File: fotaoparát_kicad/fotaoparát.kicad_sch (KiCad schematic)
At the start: 13 parts, among them IC1 W25Q256JVEIQ, J1 Conn_01x15_Pin, J2 Micro_SD_Card_Det1, Q1 AO3400A

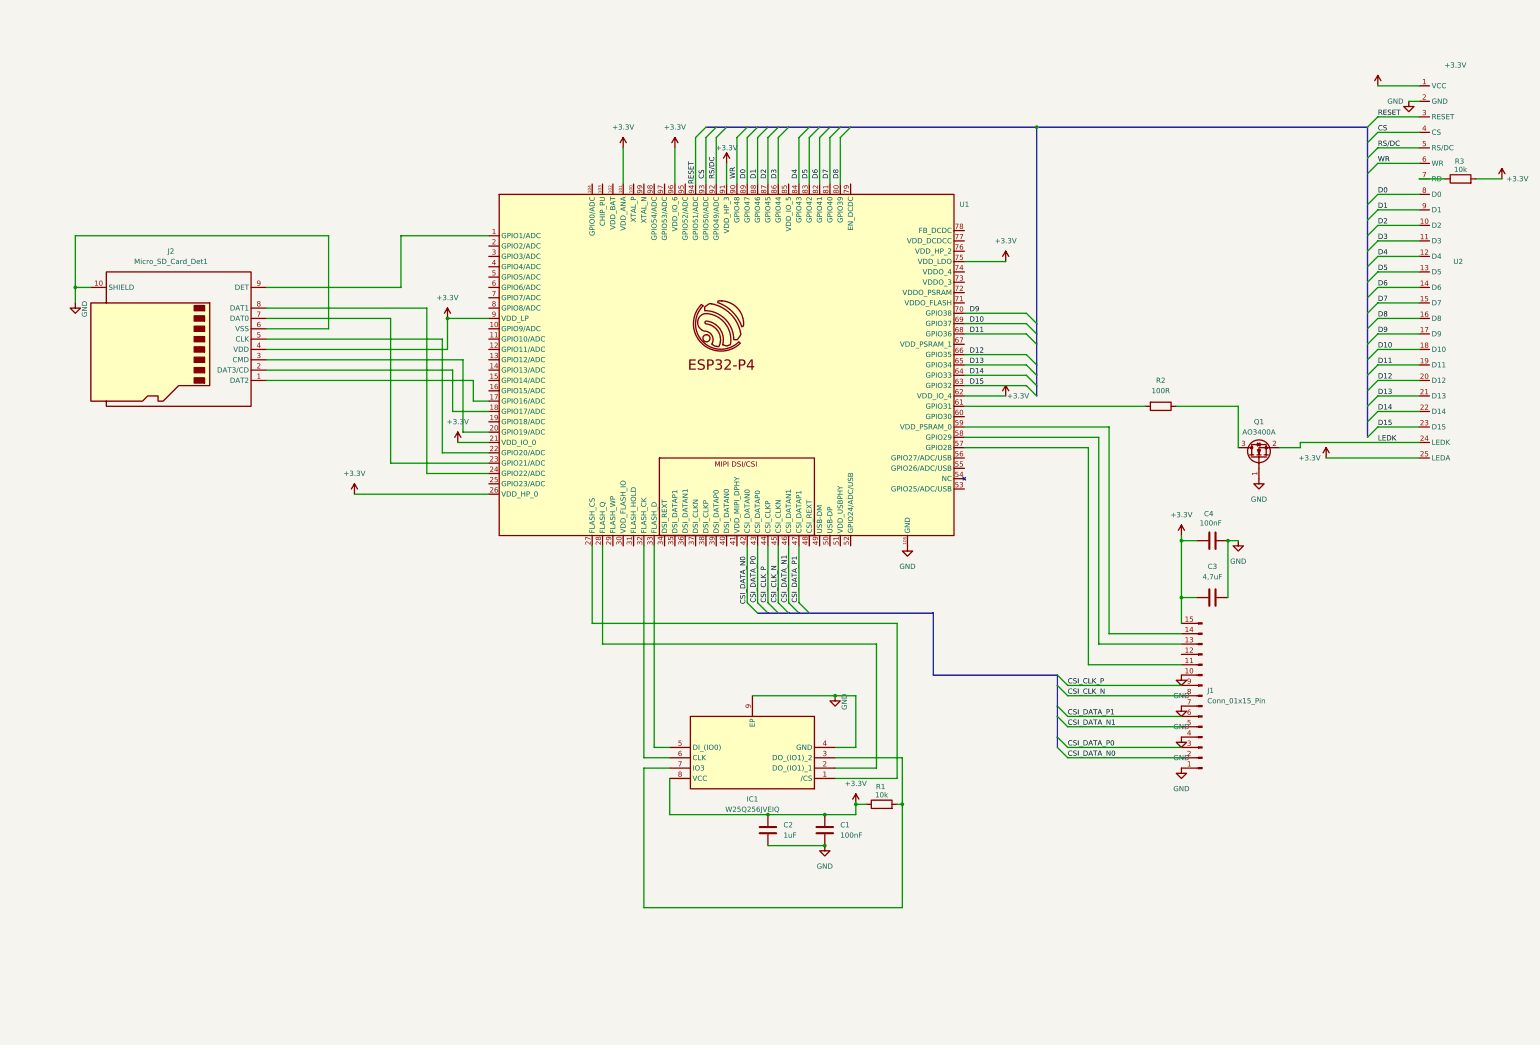
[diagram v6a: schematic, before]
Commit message: Udelal jsem znovu sd kartovy dock, tentokrat je spravne orientovany to same s konktorem na display
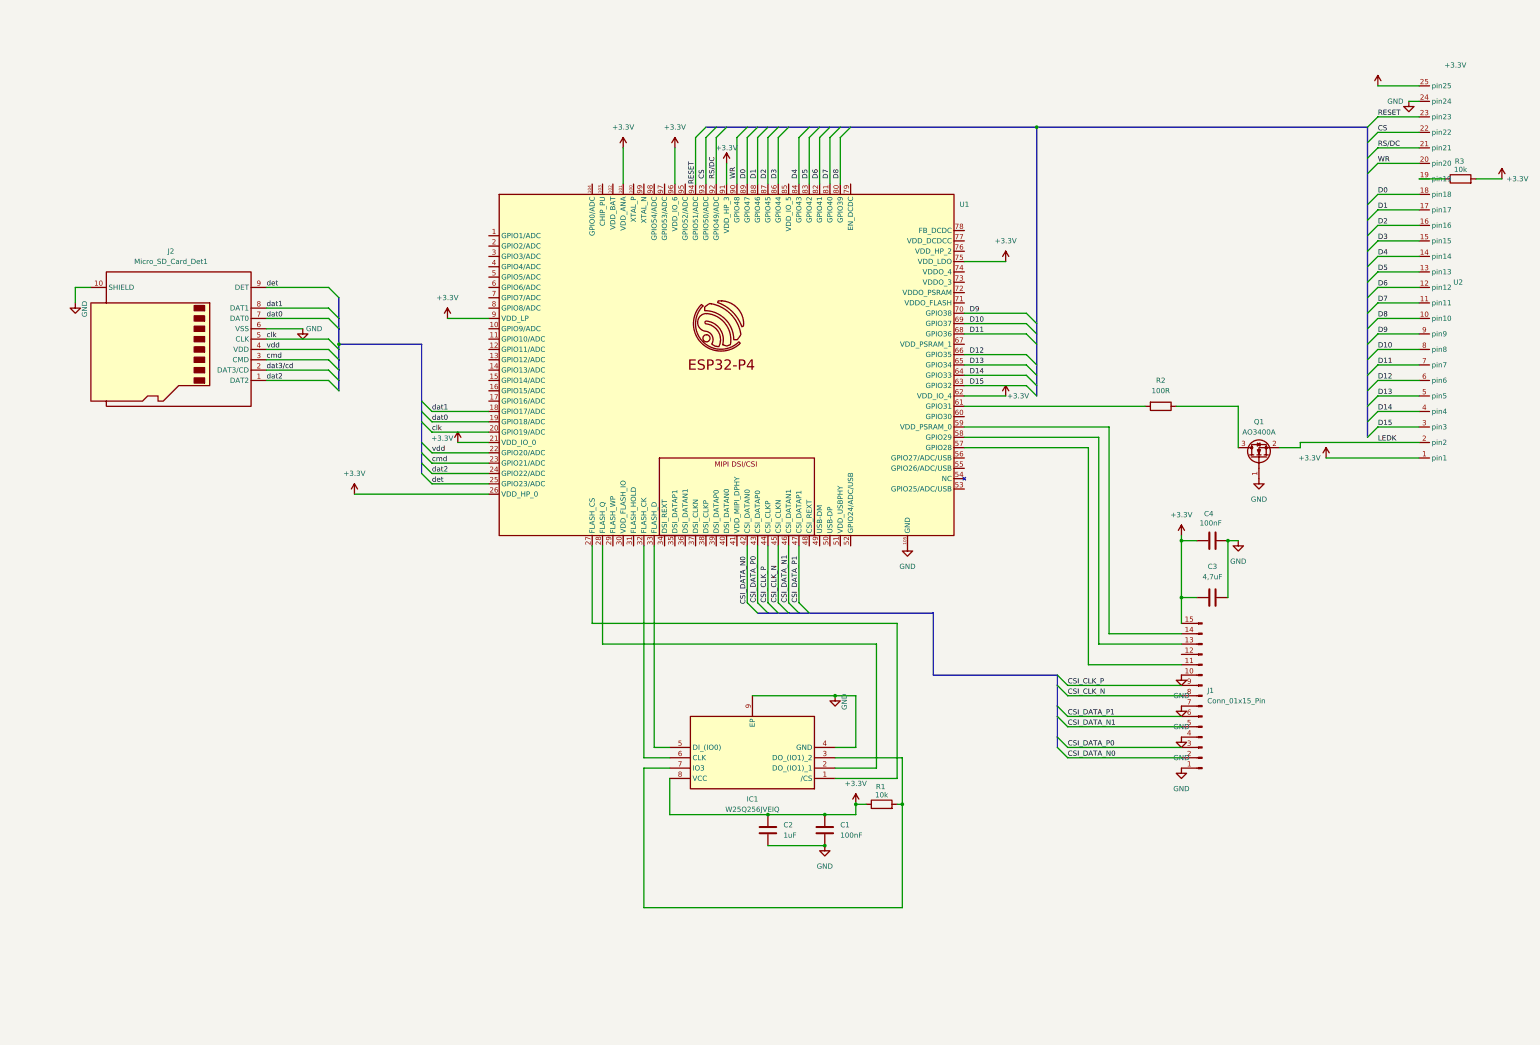
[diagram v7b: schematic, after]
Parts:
- J2: footprint Connector_Card:microSD_HC_Hirose_DM3D-SF -> Connector_Card:SD_TE_2041021
- U2: footprint stlib:ST7796s_40PIN_0.8MM -> Connector_FFC-FPC:Hirose_FH12-40S-0.5SH_1x40-1MP_P0.50mm_Horizontal
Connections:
- net +3.3V: no longer J2.4 (VDD)
- net CS: now also U2.22 (pin22); no longer U2.4 (CS)
- net D0: now also U2.18 (pin18); no longer U2.8 (D0)
- net D1: now also U2.17 (pin17); no longer U2.9 (D1)
- net D10: now also U2.8 (pin8); no longer U2.18 (D10)
- net D11: now also U2.7 (pin7); no longer U2.19 (D11)
- net D12: now also U2.6 (pin6); no longer U2.20 (D12)
- net D13: now also U2.5 (pin5); no longer U2.21 (D13)
- net D14: now also U2.4 (pin4); no longer U2.22 (D14)
- net D15: now also U2.3 (pin3); no longer U2.23 (D15)
- net D2: now also U2.16 (pin16); no longer U2.10 (D2)
- net D3: now also U2.15 (pin15); no longer U2.11 (D3)
- net D4: now also U2.14 (pin14); no longer U2.12 (D4)
- net D6: now also U2.12 (pin12); no longer U2.14 (D6)
- net D7: now also U2.11 (pin11); no longer U2.15 (D7)
- net D8: now also U2.10 (pin10); no longer U2.16 (D8)
- net D9: now also U2.9 (pin9); no longer U2.17 (D9)
- net GND: now also U2.24 (pin24); no longer U2.2 (GND)
- net LEDK: now also U2.2 (pin2); no longer U2.24 (LEDK)
- net RESET: now also U2.23 (pin23); no longer U2.3 (RESET)
- net RS/DC: now also U2.21 (pin21); no longer U2.5 (RS/DC)
- net WR: now also U2.20 (pin20); no longer U2.6 (WR)
- net at U1.1 (GPIO1/ADC): no longer J2.9 (DET)
- net at U1.17 (GPIO16/ADC): no longer J2.1 (DAT2)
- net dat1: now reaches U1.18 (GPIO17/ADC)
- net dat1: now also J2.8 (DAT1); no longer J2.2 (DAT3/CD)
- net dat0: now reaches U1.19 (GPIO18/ADC)
- net dat0: now also J2.7 (DAT0)
- net clk: now reaches U1.20 (GPIO19/ADC)
- net clk: now also J2.5 (CLK); no longer J2.3 (CMD)
- net vdd: now reaches U1.22 (GPIO20/ADC)
- net vdd: now also J2.4 (VDD); no longer J2.5 (CLK)
- net cmd: now reaches U1.23 (GPIO21/ADC)
- net cmd: now also J2.3 (CMD); no longer J2.7 (DAT0)
- net dat2: now reaches U1.24 (GPIO22/ADC)
- net dat2: now also J2.1 (DAT2); no longer J2.8 (DAT1)
- net det: now reaches U1.25 (GPIO23/ADC)
- net det: now also J2.9 (DET)
- net at R3.1: now also U2.19 (pin19); no longer U2.7 (RD)
- new net dat3/cd: J2.2 (DAT3/CD)

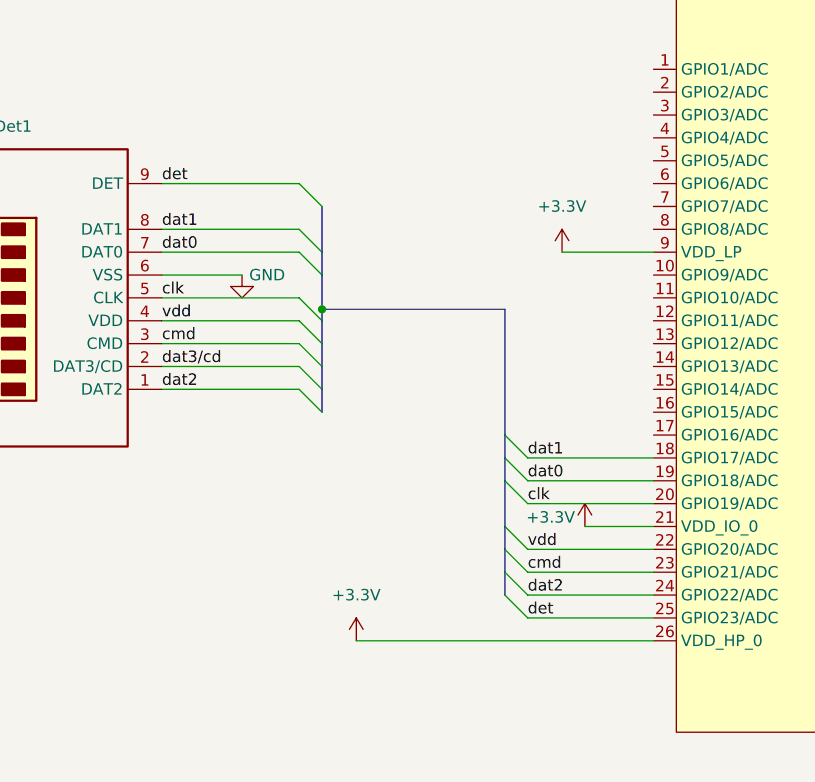
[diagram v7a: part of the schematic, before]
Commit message: Upraveni routingu pro zlepseni kvality signalu
musim predelat cely konktor na display
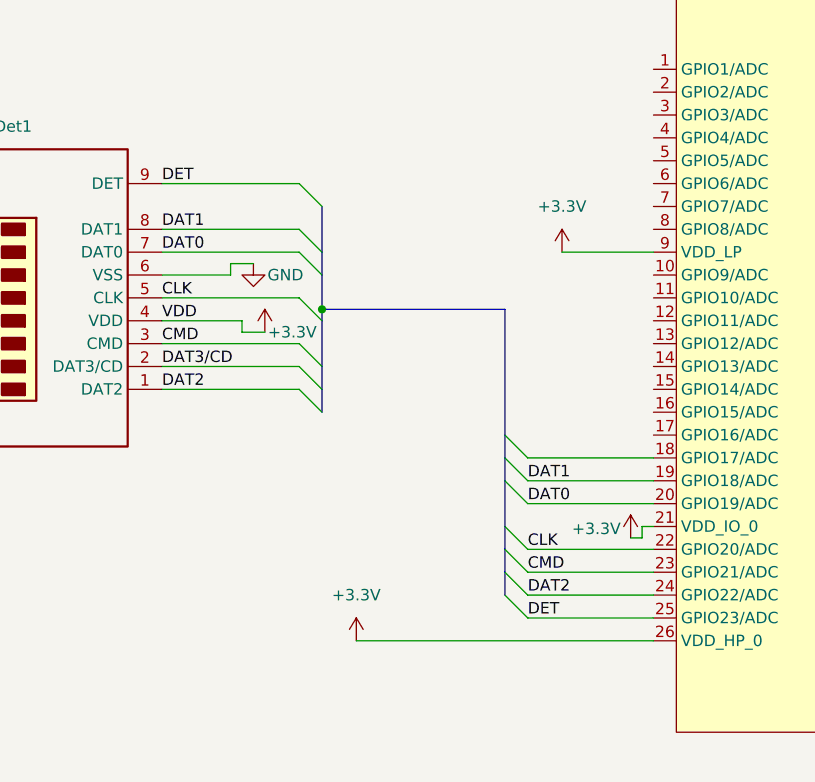
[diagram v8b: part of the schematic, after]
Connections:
- net +3.3V: now also J2.4 (VDD)
- net clk renamed CLK
- net CLK: now also U1.22 (GPIO20/ADC); no longer U1.20 (GPIO19/ADC)
- net cmd renamed CMD
- net dat0 renamed DAT0
- net DAT0: now also U1.20 (GPIO19/ADC); no longer U1.19 (GPIO18/ADC)
- net dat1: no longer names the net of U1.18 (GPIO17/ADC)
- net dat1: no longer J2.8 (DAT1)
- net dat2 renamed DAT2
- net dat3/cd renamed DAT3/CD
- net det renamed DET
- removed net vdd: J2.4 (VDD), U1.22 (GPIO20/ADC)
- new net DAT1: J2.8 (DAT1), U1.19 (GPIO18/ADC)
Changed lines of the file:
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@@
 	)
 	(bus_entry
-		(at 105.41 104.14)
-		(size 2.54 2.54)
-		(stroke
-			(width 0)
-			(type default)
-		)
-	)
-	(bus_entry
 		(at 128.27 132.08)
 		(size 2.54 2.54)
@@
 		)
 	)
-	(wire
-		(pts
-			(xy 137.16 127) (xy 144.78 127)
-		)
-		(stroke
-			(width 0)
-			(type default)
-		)
-	)
 	(bus
 		(pts
@@
 	(wire
 		(pts
+			(xy 143.51 127) (xy 144.78 127)
+		)
+		(stroke
+			(width 0)
+			(type default)
+		)
+	)
+	(wire
+		(pts
 			(xy 220.98 152.4) (xy 220.98 166.37)
 		)
@@
 		)
 	)
+	(wire
+		(pts
+			(xy 97.79 99.06) (xy 90.17 99.06)
+		)
+		(stroke
+			(width 0)
+			(type default)
+		)
+	)
 	(bus
 		(pts
@@
 	(wire
 		(pts
+			(xy 99.06 104.14) (xy 90.17 104.14)
+		)
+		(stroke
+			(width 0)
+			(type default)
+		)
+	)
+	(wire
+		(pts
 			(xy 234.95 189.23) (xy 234.95 201.93)
 		)
@@
 		)
 	)
+	(wire
+		(pts
+			(xy 142.24 128.27) (xy 143.51 128.27)
+		)
+		(stroke
+			(width 0)
+			(type default)
+		)
+	)
 	(bus
 		(pts
@@
 	(wire
 		(pts
+			(xy 97.79 97.79) (xy 97.79 99.06)
+		)
+		(stroke
+			(width 0)
+			(type default)
+		)
+	)
+	(wire
+		(pts
 			(xy 223.52 52.07) (xy 223.52 63.5)
 		)
@@
 	(wire
 		(pts
-			(xy 90.17 99.06) (xy 99.06 99.06)
+			(xy 97.79 97.79) (xy 100.33 97.79)
 		)
 		(stroke
@@
 	(wire
 		(pts
-			(xy 90.17 104.14) (xy 105.41 104.14)
+			(xy 99.06 105.41) (xy 101.6 105.41)
 		)
 		(stroke
@@
 	(bus
 		(pts
-			(xy 107.95 104.14) (xy 107.95 106.68)
+			(xy 360.68 114.3) (xy 360.68 118.11)
 		)
 		(stroke
@@
 	(bus
 		(pts
-			(xy 360.68 114.3) (xy 360.68 118.11)
+			(xy 228.6 49.53) (xy 231.14 49.53)
 		)
 		(stroke
@@
 		)
 	)
-	(bus
+	(wire
 		(pts
-			(xy 228.6 49.53) (xy 231.14 49.53)
+			(xy 314.96 173.99) (xy 297.18 173.99)
 		)
 		(stroke
@@
 	(wire
 		(pts
-			(xy 314.96 173.99) (xy 297.18 173.99)
+			(xy 99.06 105.41) (xy 99.06 104.14)
 		)
 		(stroke
@@
 	(wire
 		(pts
+			(xy 143.51 128.27) (xy 143.51 127)
+		)
+		(stroke
+			(width 0)
+			(type default)
+		)
+	)
+	(wire
+		(pts
 			(xy 363.22 39.37) (xy 373.38 39.37)
 		)
@@
 	(bus
 		(pts
-			(xy 107.95 106.68) (xy 107.95 109.22)
+			(xy 107.95 104.14) (xy 107.95 109.22)
 		)
 		(stroke
@@
 		)
 	)
-	(label "cmd"
+	(label "CMD"
 		(at 130.81 132.08 0)
 		(effects
@@
 		)
 	)
-	(label "vdd"
-		(at 130.81 129.54 0)
-		(effects
-			(font
-				(size 1.27 1.27)
-			)
-			(justify left bottom)
-		)
-	)
-	(label "clk"
-		(at 130.81 124.46 0)
-		(effects
-			(font
-				(size 1.27 1.27)
-			)
-			(justify left bottom)
-		)
-	)
-	(label "dat0"
-		(at 130.81 121.92 0)
+	(label "DAT2"
+		(at 130.81 134.62 0)
 		(effects
 			(font
@@
 		)
 	)
-	(label "dat2"
-		(at 130.81 134.62 0)
+	(label "DET"
+		(at 130.81 137.16 0)
 		(effects
 			(font
@@
 		)
 	)
-	(label "det"
-		(at 130.81 137.16 0)
+	(label "DAT3{slash}CD"
+		(at 90.17 109.22 0)
 		(effects
 			(font
@@
 		)
 	)
-	(label "dat3{slash}cd"
-		(at 90.17 109.22 0)
+	(label "D10"
+		(at 262.89 97.79 0)
 		(effects
 			(font
@@
 		)
 	)
-	(label "D10"
-		(at 262.89 97.79 0)
+	(label "DAT2"
+		(at 90.17 111.76 0)
 		(effects
 			(font
@@
 		)
 	)
-	(label "dat2"
-		(at 90.17 111.76 0)
+	(label "CLK"
+		(at 130.81 129.54 0)
 		(effects
 			(font
@@
 		)
 	)
-	(label "cmd"
+	(label "CMD"
 		(at 90.17 106.68 0)
 		(effects
@@
 		)
 	)
-	(label "vdd"
+	(label "VDD"
 		(at 90.17 104.14 0)
 		(effects
@@
 		)
 	)
-	(label "clk"
+	(label "CLK"
 		(at 90.17 101.6 0)
 		(effects
@@
 		)
 	)
-	(label "dat0"
+	(label "DAT0"
 		(at 90.17 96.52 0)
 		(effects
@@
 		)
 	)
-	(label "dat1"
+	(label "DAT1"
 		(at 90.17 93.98 0)
 		(effects
@@
 		)
 	)
-	(label "det"
+	(label "DET"
 		(at 90.17 88.9 0)
 		(effects
@@
 		)
 	)
-	(label "dat1"
-		(at 130.81 119.38 0)
+	(label "D7"
+		(at 228.6 62.23 90)
 		(effects
 			(font
@@
 		)
 	)
-	(label "D7"
-		(at 228.6 62.23 90)
+	(label "CSI_CLK_P"
+		(at 213.36 166.37 90)
 		(effects
 			(font
@@
 		)
 	)
-	(label "CSI_CLK_P"
-		(at 213.36 166.37 90)
+	(label "DAT1"
+		(at 130.81 121.92 0)
 		(effects
 			(font
@@
 		)
 	)
+	(label "DAT0"
+		(at 130.81 124.46 0)
+		(effects
+			(font
+				(size 1.27 1.27)
+			)
+			(justify left bottom)
+		)
+	)
 	(label "CSI_DATA_P1"
 		(at 287.02 194.31 0)
@@
 	(symbol
 		(lib_id "power:GND")
-		(at 99.06 99.06 0)
+		(at 100.33 97.79 0)
 		(unit 1)
 		(exclude_from_sim no)
@@
 		(dnp no)
 		(property "Reference" "#PWR023"
-			(at 99.06 105.41 0)
+			(at 100.33 104.14 0)
 			(effects
 				(font
@@
 		)
 		(property "Value" "GND"
-			(at 101.854 99.06 0)
+			(at 103.886 99.06 0)
 			(effects
 				(font
@@
 		)
 		(property "Footprint" ""
-			(at 99.06 99.06 0)
+			(at 100.33 97.79 0)
 			(effects
 				(font
@@
 		)
 		(property "Datasheet" ""
-			(at 99.06 99.06 0)
+			(at 100.33 97.79 0)
 			(effects
 				(font
@@
 		)
 		(property "Description" "Power symbol creates a global label with name \"GND\" , ground"
-			(at 99.06 99.06 0)
+			(at 100.33 97.79 0)
 			(effects
 				(font
@@
 	(symbol
 		(lib_id "power:+3.3V")
-		(at 137.16 127 0)
+		(at 142.24 128.27 0)
 		(unit 1)
 		(exclude_from_sim no)
@@
 		(dnp no)
 		(property "Reference" "#PWR06"
-			(at 137.16 130.81 0)
+			(at 142.24 132.08 0)
 			(effects
 				(font
@@
 		)
 		(property "Value" "+3.3V"
-			(at 133.35 125.984 0)
+			(at 138.43 127.254 0)
 			(effects
 				(font
@@
 		)
 		(property "Footprint" ""
-			(at 137.16 127 0)
+			(at 142.24 128.27 0)
 			(effects
 				(font
@@
 		)
 		(property "Datasheet" ""
-			(at 137.16 127 0)
+			(at 142.24 128.27 0)
 			(effects
 				(font
@@
 		)
 		(property "Description" "Power symbol creates a global label with name \"+3.3V\""
-			(at 137.16 127 0)
+			(at 142.24 128.27 0)
 			(effects
 				(font
@@
 					(unit 1)
 				)
+			)
+		)
+	)
+	(symbol
+		(lib_id "power:+3.3V")
+		(at 101.6 105.41 0)
+		(unit 1)
+		(exclude_from_sim no)
+		(in_bom yes)
+		(on_board yes)
+		(dnp no)
+		(property "Reference" "#PWR024"
+			(at 101.6 109.22 0)
+			(effects
+				(font
+					(size 1.27 1.27)
+				)
+				(hide yes)
+			)
+		)
+		(property "Value" "+3.3V"
+			(at 104.648 105.41 0)
+			(effects
+				(font
+					(size 1.27 1.27)
+				)
+			)
+		)
+		(property "Footprint" ""
+			(at 101.6 105.41 0)
+			(effects
+				(font
+					(size 1.27 1.27)
+				)
+				(hide yes)
+			)
+		)
+		(property "Datasheet" ""
+			(at 101.6 105.41 0)
+			(effects
+				(font
+					(size 1.27 1.27)
+				)
+				(hide yes)
+			)
+		)
+		(property "Description" "Power symbol creates a global label with name \"+3.3V\""
+			(at 101.6 105.41 0)
+			(effects
+				(font
+					(size 1.27 1.27)
+				)
+				(hide yes)
+			)
+		)
+		(pin "1"
+		)
+		(instances
+			(project ""
+				(path "/0ab33720-0b6a-449c-80c0-2b7abe4d9450"
+					(reference "#PWR024")
+					(unit 1)
+				)
